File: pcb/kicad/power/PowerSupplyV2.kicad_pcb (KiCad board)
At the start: 2 copper layers, 44 parts, among them J1 12VWallWartVin, J2 AudioInput, J3 BackUpPower12V, J4 Display5V, J5 WallWartACin, J6 120VAC, J7 Uc3.3VSignal, J8 Ucontroller3.3, U1 LM386, U3 LM2574

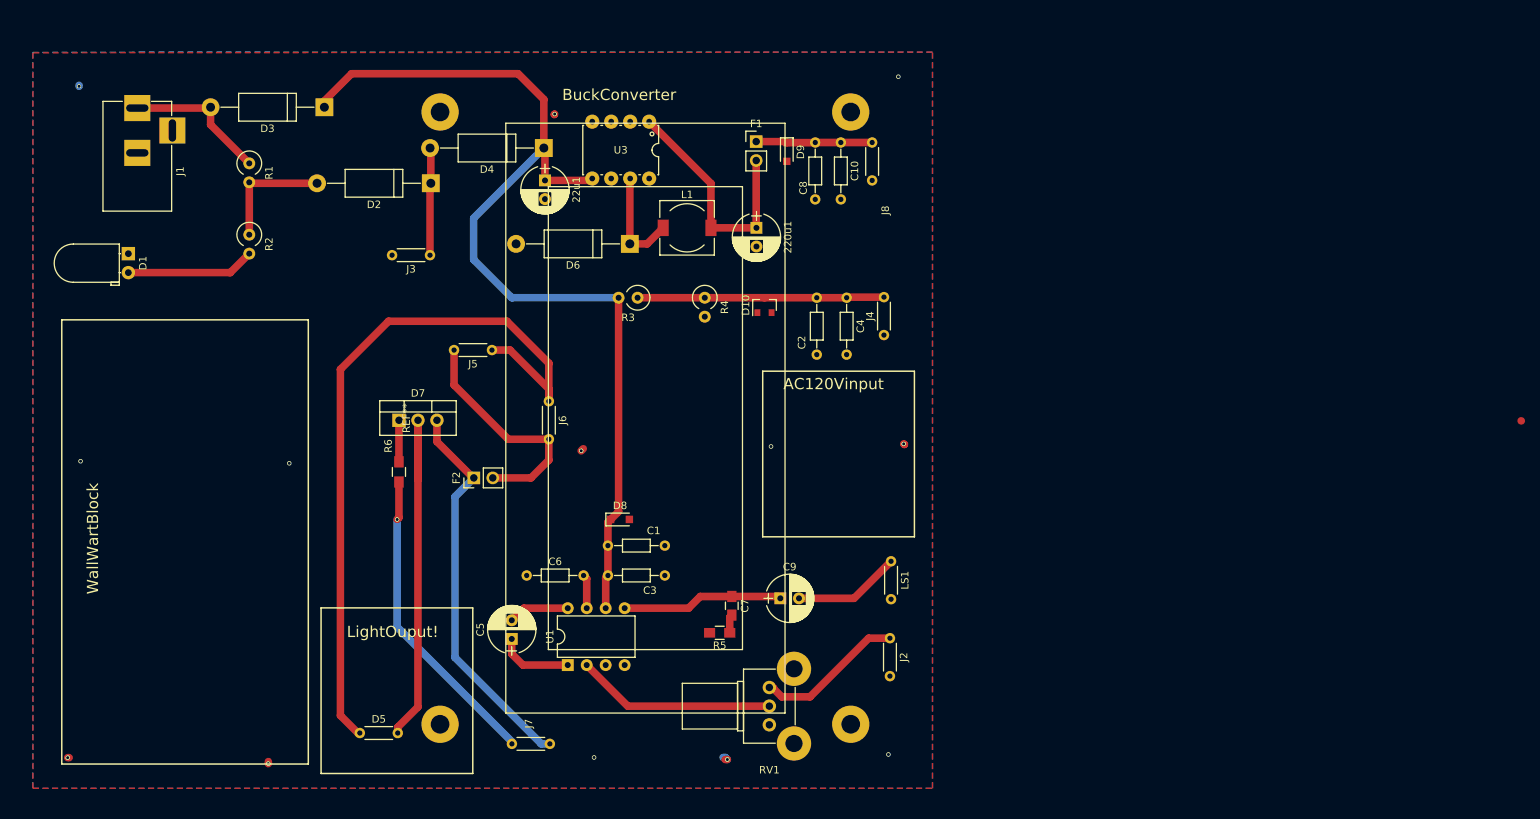
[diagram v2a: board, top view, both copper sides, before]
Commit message: Finish new base station and tile boards
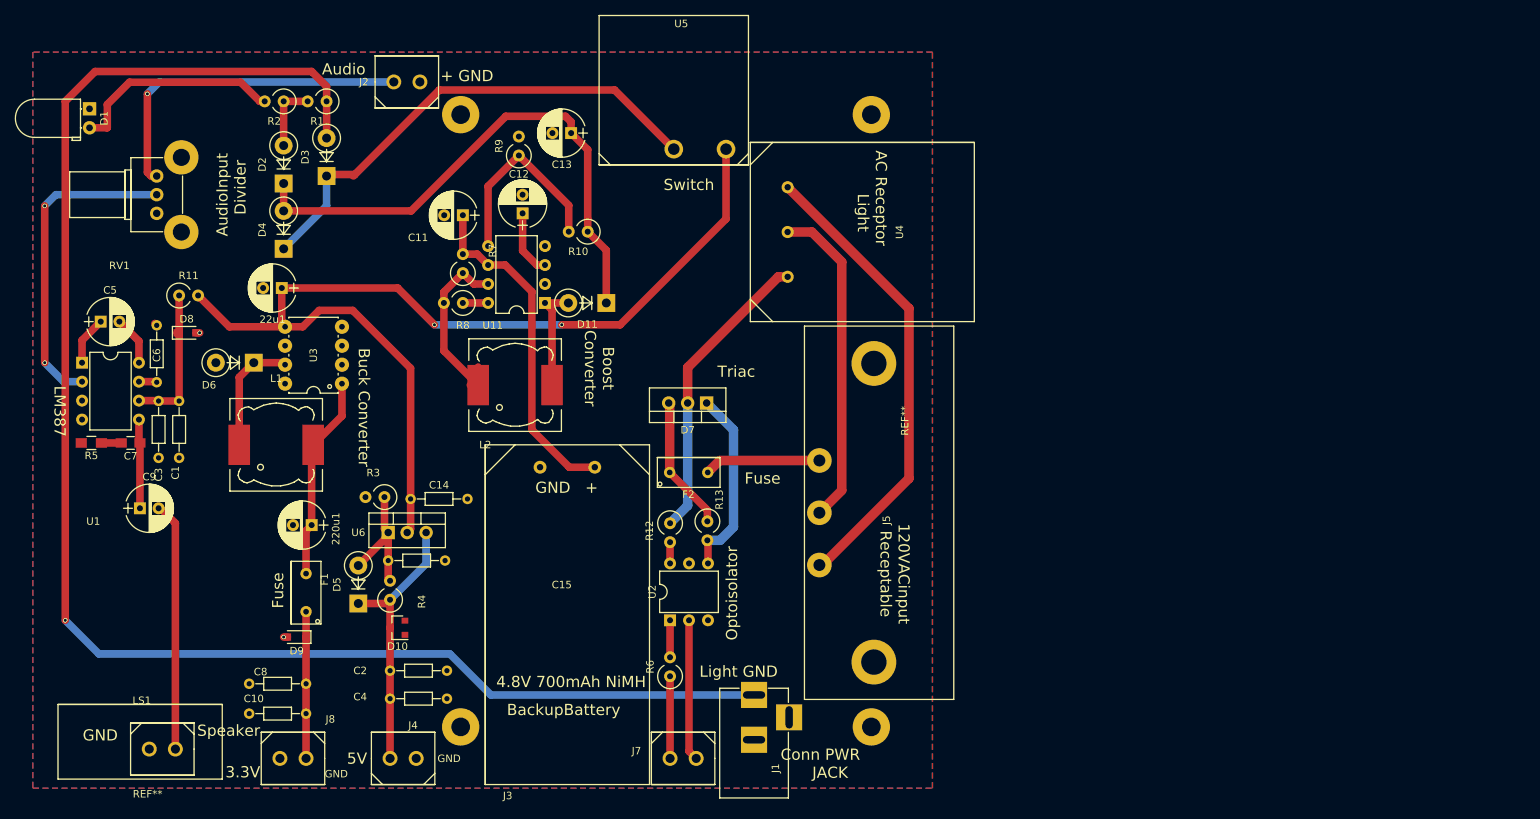
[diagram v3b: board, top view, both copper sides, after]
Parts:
- removed J6: 120VAC, Resistors_THT:R_Axial_DIN0204_L3.6mm_D1.6mm_P5.08mm_Horizontal
- removed the REF** at (107.5, 74.4)
- added C11: 100uF, Capacitors_THT:CP_Radial_D6.3mm_P2.50mm, F.Cu at (83.0, 47.2)
- added C12: 1500pF, Capacitors_THT:CP_Radial_D6.3mm_P2.50mm, F.Cu at (91.0, 47.0)
- added C13: 330uF, Capacitors_THT:CP_Radial_D6.3mm_P2.50mm, F.Cu at (97.5, 36.2)
- added C14: 0.1u, Resistors_THT:R_Axial_DIN0204_L3.6mm_D1.6mm_P7.62mm_Horizontal, F.Cu at (76.0, 85.2)
- added C15: 10uF, Resistors_THT:R_Axial_DIN0204_L3.6mm_D1.6mm_P7.62mm_Horizontal, F.Cu at (73.0, 93.5)
- added D11: 1N5819, Diodes_THT:D_DO-15_P5.08mm_Vertical_KathodeUp, F.Cu at (102.2, 59.0)
- added L2: 160uH, Choke_SMD:Choke_SMD_12x12mm_h4.5mm, F.Cu at (90.0, 70.0)
- added R10: 10k, Resistors_THT:R_Axial_DIN0309_L9.0mm_D3.2mm_P2.54mm_Vertical, F.Cu at (99.7, 49.5)
- added R11: 1k, Resistors_THT:R_Axial_DIN0309_L9.0mm_D3.2mm_P2.54mm_Vertical, F.Cu at (45.0, 58.0)
- added R12: 180, Resistors_THT:R_Axial_DIN0309_L9.0mm_D3.2mm_P2.54mm_Vertical, F.Cu at (110.8, 88.5)
- added R13: 1k, Resistors_THT:R_Axial_DIN0309_L9.0mm_D3.2mm_P2.54mm_Vertical, F.Cu at (115.8, 88.2)
- added R7: 0.22, Resistors_THT:R_Axial_DIN0309_L9.0mm_D3.2mm_P2.54mm_Vertical, F.Cu at (83.0, 55.0)
- added R8: 180, Resistors_THT:R_Axial_DIN0309_L9.0mm_D3.2mm_P2.54mm_Vertical, F.Cu at (83.0, 59.0)
- added R9: 1k, Resistors_THT:R_Axial_DIN0309_L9.0mm_D3.2mm_P2.54mm_Vertical, F.Cu at (90.5, 39.2)
- added REF**: SpeakerTemp rCDM-20008, SpeakerTemp, F.Cu at (28.8, 122.8)
- added REF**: CFAH1604A, Footprints:CFAH1604A, F.Cu at (110.2, 74.8)
- added U11: BoostConv, Housings_DIP:DIP-8_W7.62mm, F.Cu at (94.0, 59.0)
- added U2: MOC3043M, Housings_DIP:DIP-6_W7.62mm, F.Cu at (110.8, 101.5)
- added U4: ExternalLightACPlug, Footprints:739W-X203, F.Cu at (121.5, 37.5)
- added U5: Switch, Footprints:Switch, F.Cu at (101.2, 40.5)
- added U6: LM317K, TO_SOT_Packages_THT:TO-220_Vertical, F.Cu at (73.0, 89.8)
- D2, D3, D4, D6: footprint Diodes_THT:D_DO-15_P15.24mm_Horizontal -> Diodes_THT:D_DO-15_P5.08mm_Vertical_KathodeUp
- D5: value 6.6WLED -> 1N4002; footprint Resistors_THT:R_Axial_DIN0204_L3.6mm_D1.6mm_P5.08mm_Horizontal -> Diodes_THT:D_DO-15_P5.08mm_Vertical_KathodeUp
- F1: value Fuse1Amp -> 0.5Amp; footprint Pin_Headers:Pin_Header_Straight_1x02_Pitch2.54mm -> Footprints:FuseTH500mA
- F2: value 3Amps -> 0.5Amps; footprint Pin_Headers:Pin_Header_Straight_1x02_Pitch2.54mm -> Footprints:FuseTH500mA
- J2, J4, J7, J8, LS1: footprint Resistors_THT:R_Axial_DIN0204_L3.6mm_D1.6mm_P5.08mm_Horizontal -> Footprints:BlockTerminal3.5mm
- J3: footprint Resistors_THT:R_Axial_DIN0204_L3.6mm_D1.6mm_P5.08mm_Horizontal -> Footprints:NIMH4.8V
- J5: value WallWartACin -> 120Vinput; footprint Resistors_THT:R_Axial_DIN0204_L3.6mm_D1.6mm_P5.08mm_Horizontal -> Footprints:703w0053
- L1: footprint Choke_SMD:Choke_SMD_7.3x7.3_H3.5 -> Choke_SMD:Choke_SMD_12x12mm_h4.5mm
- R3: value 160 -> 750
- R4: value 120 -> 240
- R6: value 120 -> 660; footprint Resistors_SMD:R_0805_HandSoldering -> Resistors_THT:R_Axial_DIN0309_L9.0mm_D3.2mm_P2.54mm_Vertical
- moved J1 114.0 mm to (122.0, 111.5)
- moved J8 108.4 mm to (62.0, 120.0), turned to 180 degrees
- moved RV1 106.9 mm to (42.0, 42.0)
- moved C10 104.8 mm to (62.0, 114.0), turned to 180 degrees
- moved J2 99.8 mm to (73.8, 29.4), turned to 0 degrees
- moved C8 99.5 mm to (62.0, 110.0), turned to 180 degrees
- moved LS1 99.1 mm to (44.5, 118.8), turned to 180 degrees
- moved D9 92.4 mm to (60.8, 103.8), turned to 180 degrees
- moved R5 87.9 mm to (33.2, 77.8)
- moved J4 87.1 mm to (73.2, 120.0), turned to 0 degrees
- moved F1 87.0 mm to (64.0, 102.0), turned to 90 degrees
- moved C9 86.6 mm to (39.8, 86.5)
- moved C7 83.4 mm to (38.5, 77.8), turned to 180 degrees
- moved C4 81.4 mm to (73.2, 112.0), turned to 0 degrees
- moved U1 76.6 mm to (32.0, 67.0), turned to 0 degrees
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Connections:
- C1 pad 2: Net-(22u1-Pad1) -> Net-(C1-Pad2)
- C3 pad 2: Net-(22u1-Pad1) -> Net-(C1-Pad2)
- D2 pad 1: Net-(D2-Pad1) -> Net-(C13-Pad1)
- D3 pad 1: Net-(22u1-Pad1) -> Net-(D3-Pad1)
- D4 pad 1: Net-(22u1-Pad1) -> Net-(D3-Pad1)
- D4 pad 2: Net-(D2-Pad1) -> Net-(C13-Pad1)
- D5 pad 1: Net-(D5-Pad1) -> Net-(C2-Pad1)
- D5 pad 2: Net-(D5-Pad2) -> Net-(C15-Pad1)
- D7 pad 2: Net-(D5-Pad2) -> Net-(D7-Pad2)
- D8 pad 1: Net-(22u1-Pad1) -> Net-(C1-Pad2)
- J3 pad 1: Net-(D2-Pad1) -> Net-(C11-Pad1)
- J4 pad 1: GND -> Net-(C2-Pad1)
- J4 pad 2: Net-(C2-Pad1) -> GND
- J5 pad 1: Net-(D5-Pad1) -> Net-(J5-Pad1)
- J7 pad 1: Net-(D7-Pad3) -> Net-(J7-Pad1)
- J8 pad 1: GND -> Net-(C10-Pad1)
- J8 pad 2: Net-(C10-Pad1) -> GND
- R3 pad 1: Net-(C2-Pad1) -> Net-(C15-Pad1)
- R3 pad 2: Net-(22u1-Pad1) -> GND
- R4 pad 2: GND -> Net-(C15-Pad1)
- R6 pad 2: Net-(D7-Pad1) -> Net-(R6-Pad2)
- U1 pad 4: Net-(U1-Pad4) -> GND
- U1 pad 6: Net-(22u1-Pad1) -> Net-(C1-Pad2)
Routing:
- net Net-(D3-Pad2): track 20.1 -> 210.3 mm, vias 0 -> 1
- net Net-(D5-Pad1): track 99.4 -> 0.00 mm
- net Net-(C13-Pad1): track 0.00 -> 73.9 mm
- net Net-(D3-Pad1): track 0.00 -> 67.5 mm
- net Net-(J5-Pad1): track 0.00 -> 62.5 mm
- net Net-(D5-Pad2): track 51.0 -> 0.00 mm
- net Net-(C11-Pad1): track 0.00 -> 45.5 mm
- net Net-(J5-Pad3): track 0.00 -> 43.7 mm
- net Net-(D7-Pad2): track 0.00 -> 40.3 mm
- net Net-(D7-Pad3): track 52.7 -> 18.0 mm
- net Net-(J7-Pad2): track 41.5 -> 11.0 mm, vias 1 -> 0
- net Net-(L2-Pad1): track 0.00 -> 27.3 mm
- net Net-(R10-Pad2): track 0.00 -> 26.8 mm
- net Net-(J2-Pad1): track 21.1 -> 45.6 mm, vias 0 -> 1
- net Net-(D7-Pad1): track 5.57 -> 25.5 mm
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- added copper zone on F.Cu, net (none)
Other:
- board text added: "+ GND"
- board text added: "120VACinput Receptable"
- board text added: "3.3V"
- board text added: "4.8V 700mAh NiMH"
- board text added: "5V"
- board text added: "AC Receptor Light"
- board text added: "ACLightOpening"
- board text added: "ACinputConnectorOpenning"
- board text added: "Audio"
- board text added: "AudioInput Divider"
- board text added: "BackupBattery"
- board text added: "Boost Converter"
- board text added: "Buck Converter"
- board text added: "Conn PWR JACK"
- board text added: "FrontSide"
- board text added: "Fuse"
- board text added: "GND"
- board text added: "GND +"
- board text added: "Jack Barrel Opening"
- board text added: "LM387"
- board text added: "Light GND"
- board text added: "OpeningForSpeaker"
- board text added: "Optoisolator"
- board text added: "Speaker"
- board text added: "Switch"
- board text added: "Switch Opening"
- board text added: "Triac"
- board text removed: "AC120Vinput"
- board text removed: "BuckConverter"
- board text removed: "LightOuput!"
- board text removed: "WallWartBlock"
